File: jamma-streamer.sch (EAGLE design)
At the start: 49 parts, among them IC1 LM7805, J1 Audio line out, J2 ICSP, J3 SDCARD, J4 USB, T1 TY-145P, T2 TY-145P, U1 CD74HC165MD16-M, U2 ATMEGA328PB-AUR, U3 74HC4050D, U4 TLV757X / LP298X, U5 CD74HC165MD16-M, U6 CD74HC165MD16-M, U7 FT232RL, Y1 16MHz

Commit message: New version including RTC and better alim
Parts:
- added B1: S8411-45R, S8411R:S8411-45R
- added C11, C12, C13: 0.1uF/16V, CMS:KEMET-C1210C104K4J
- added C8: 10uF/10V, CMS:KEMET-C1210C106K8N
- added JP1: (no value), pinhead:PINHD-1X5
- added R6, R7, R8, R9: 10K, CMS:BOURNS-CRM2512AJW103ELF
- added SJ1: (no value), jumper:SJW
- added U10: LM358DTD8-M, LM358D:LM358DTD8-M
- added U8: DS3231SNT&R21-0042B_16-M, DS3231:DS3231SNT&R21-0042B_16-M
- added U9: NDT2955SOT-223-M, NDT2955:NDT2955SOT-223-M
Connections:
- net N$13 renamed PB6
- removed net N$11: C7.P$2, U7.3V3OUT
- new net CMD_GATE: U10.2IN-, U10.2OUT, U9.G
- new net CMP: C12.P$1, R8.P$1, R9.P$2, U10.1IN+
- new net DTR: C11.P$1, JP1.4, U7.DTR
- new net N$13: C11.P$2, SJ1.1
- new net N$31: B1.+, U8.VBAT
- new net PB7: C2.P$1, U2.PB7, Y1.1
- new net RTS: JP1.3, U7.RTS
- new net SCL: R6.P$2, U2.PC5, U8.SCL
- new net SDA: R7.P$2, U2.PC4, U8.SDA
- new net USBVCC: C10.P$1, C9.P$1, F1.P$2, U7.VCC, U9.D
- new net VCC33: C7.P$2, U10.1IN-, U7.3V3OUT
- new net VIN: C5.P$1, D5.P$1, IC1.VI, R8.P$2
- net CS: now also JP1.5; no longer C2.P$1, U2.PB7, Y1.1
- net FTDI_RXD: now also JP1.2
- net FTDI_TXD: now also JP1.1
- net GND: now also B1.-, C12.P$2, C13.P$2, C8.P$2, R9.P$1, U10.GND, U8.GND
- net JAMMA+12V: now also D5.P$2; no longer C5.P$1, IC1.VI
- net N$23: now also U10.1OUT, U10.2IN+; no longer D5.P$2, IC1.VO
- net RESET: now also SJ1.2
- net VCC: now also C13.P$1, C8.P$1, IC1.VO, R6.P$1, R7.P$1, U10.VCC, U8.VCC, U9.S; no longer C10.P$1, C9.P$1, D5.P$1, F1.P$2, U7.VCC
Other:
- note added: "CS = PB2 = Pin 10 Used to send reset signal when using ISP if using this atmega to program others"
- note added: "In the arduino code: Pin0=d0 Pin1 = d1 Pin2 = d2 ..."
- note added: "In the arduino code: Pin16=d0 Pin17 = d1 Pin18 = d2 ..."
- note added: "In the arduino code: Pin8=d0 Pin9 = d1 Pin10 = d2 ..."

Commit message: Updating readme with more info
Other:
- note added: "CS = PB2 = Pin 10 Used by ArduinoISP sketch to send a reset signal when using this atmega as ISP programmer"
- note added: "In the arduino code: Pin0 = d0 Pin1 = d1 Pin2 = d2 ..."
- note added: "In the arduino code: Pin16 = d0 Pin17 = d1 Pin18 = d2 ..."
- note added: "In the arduino code: Pin8 = d0 Pin9 = d1 Pin10 = d2 ..."
- note added: "MISO SCK RST"
- note added: "VCC MOSI GND"
- note removed: "CS = PB2 = Pin 10 Used to send reset signal when using ISP if using this atmega to program others"
- note removed: "In the arduino code: Pin0=d0 Pin1 = d1 Pin2 = d2 ..."
- note removed: "In the arduino code: Pin16=d0 Pin17 = d1 Pin18 = d2 ..."
- note removed: "In the arduino code: Pin8=d0 Pin9 = d1 Pin10 = d2 ..."
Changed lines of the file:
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@@
 <?xml version="1.0" encoding="utf-8"?>
 <!DOCTYPE eagle SYSTEM "eagle.dtd">
-<eagle version="9.2.2">
+<eagle version="9.6.2">
 <drawing>
 <settings>
@@
 PD6 = Data
 PD7 = Clock</text>
+<text x="7.62" y="106.68" size="1.778" layer="91">MISO
+SCK
+RST</text>
+<text x="20.32" y="106.68" size="1.778" layer="91">VCC
+MOSI
+GND</text>
 </plain>
 <instances>
@@
 <segment>
 <pinref part="SUPPLY9" gate="G$1" pin="VCC"/>
-<wire x1="111.76" y1="101.6" x2="111.76" y2="106.68" width="0.1524" layer="91"/>
+<wire x1="111.76" y1="99.06" x2="111.76" y2="106.68" width="0.1524" layer="91"/>
 <pinref part="U2" gate="G$1" pin="VCC"/>
 <wire x1="91.44" y1="99.06" x2="99.06" y2="99.06" width="0.1524" layer="91"/>
 <wire x1="99.06" y1="99.06" x2="111.76" y2="99.06" width="0.1524" layer="91"/>
-<wire x1="111.76" y1="99.06" x2="111.76" y2="101.6" width="0.1524" layer="91"/>
 <pinref part="U2" gate="G$1" pin="AVCC"/>
 <wire x1="91.44" y1="101.6" x2="99.06" y2="101.6" width="0.1524" layer="91"/>
@@
 <text x="-45.72" y="207.01" size="1.778" layer="91" font="vector">Jamma is HIGH when not pressed (~3V)
 and LOW when pressed !</text>
-<text x="96.52" y="119.38" size="1.27" layer="91">In the arduino code:
-Pin0=d0
+<text x="96.52" y="119.38" size="1.27" layer="91" font="fixed">In the arduino code:
+Pin0 = d0
 Pin1 = d1
 Pin2 = d2
 ...</text>
-<text x="99.06" y="160.02" size="1.27" layer="91">In the arduino code:
-Pin8=d0
-Pin9 = d1
+<text x="99.06" y="160.02" size="1.27" layer="91" font="fixed">In the arduino code:
+Pin8  = d0
+Pin9  = d1
 Pin10 = d2
 ...</text>
-<text x="88.9" y="200.66" size="1.27" layer="91">In the arduino code:
-Pin16=d0
+<text x="88.9" y="200.66" size="1.27" layer="91" font="fixed">In the arduino code:
+Pin16 = d0
 Pin17 = d1
 Pin18 = d2
@@
 <description>USB input</description>
 <plain>
-<text x="104.14" y="76.2" size="1.778" layer="91">CS = PB2 = Pin 10
-Used to send reset signal when using ISP
-if using this atmega to program others</text>
+<text x="104.14" y="73.66" size="1.778" layer="91">CS = PB2 = Pin 10
+Used by ArduinoISP sketch to send a reset
+signal when using this atmega as ISP programmer</text>
 </plain>
 <instances>

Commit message: New README, new schematic after burn fixing
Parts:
- SJ1: device jumper:SJW -> jumper:SJ
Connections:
- removed net VCCIO: R4.P$2, R5.P$2, U7.VCCIO
- net USBVCC: now also R4.P$2, R5.P$2, U7.VCCIO
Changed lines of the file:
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@@
 <layer number="1" name="Top" color="4" fill="1" visible="no" active="no"/>
 <layer number="2" name="Route2" color="16" fill="1" visible="no" active="no"/>
+<layer number="3" name="Route3" color="4" fill="3" visible="no" active="no"/>
+<layer number="4" name="Route4" color="1" fill="4" visible="no" active="no"/>
+<layer number="5" name="Route5" color="4" fill="4" visible="no" active="no"/>
+<layer number="6" name="Route6" color="1" fill="8" visible="no" active="no"/>
+<layer number="7" name="Route7" color="4" fill="8" visible="no" active="no"/>
+<layer number="8" name="Route8" color="1" fill="2" visible="no" active="no"/>
+<layer number="9" name="Route9" color="4" fill="2" visible="no" active="no"/>
+<layer number="10" name="Route10" color="1" fill="7" visible="no" active="no"/>
+<layer number="11" name="Route11" color="4" fill="7" visible="no" active="no"/>
+<layer number="12" name="Route12" color="1" fill="5" visible="no" active="no"/>
+<layer number="13" name="Route13" color="4" fill="5" visible="no" active="no"/>
+<layer number="14" name="Route14" color="1" fill="6" visible="no" active="no"/>
 <layer number="15" name="Route15" color="23" fill="1" visible="no" active="no"/>
 <layer number="16" name="Bottom" color="1" fill="1" visible="no" active="no"/>
@@
 <part name="R5" library="CMS" deviceset="BOURNS-652CHP0603FX1001ELF" device="" value="1K"/>
 <part name="D4-TX" library="CMS" deviceset="604-APTD1608LCGCK" device="" value="Green"/>
-<part name="SUPPLY16" library="SparkFun-PowerSymbols" library_urn="urn:adsk.eagle:library:530" deviceset="VCCIO" device=""/>
-<part name="SUPPLY17" library="SparkFun-PowerSymbols" library_urn="urn:adsk.eagle:library:530" deviceset="VCCIO" device=""/>
 <part name="D5" library="RRE07VTM4SFHTR" deviceset="RRE07VTM4SFHTR" device="" value="RRE07VTM4SFHTR"/>
 <part name="GND24" library="SparkFun-PowerSymbols" library_urn="urn:adsk.eagle:library:530" deviceset="GND" device=""/>
@@
 <part name="C11" library="CMS" deviceset="KEMET-C1210C104K4J" device="" value="0.1uF/16V"/>
 <part name="JP1" library="pinhead" library_urn="urn:adsk.eagle:library:325" deviceset="PINHD-1X5" device="" package3d_urn="urn:adsk.eagle:package:22469/2"/>
-<part name="SJ1" library="jumper" library_urn="urn:adsk.eagle:library:252" deviceset="SJ" device="W" package3d_urn="urn:adsk.eagle:package:15507/1"/>
+<part name="SJ1" library="jumper" library_urn="urn:adsk.eagle:library:252" deviceset="SJ" device="" package3d_urn="urn:adsk.eagle:package:15471/1"/>
 <part name="U8" library="DS3231" deviceset="DS3231SNT&amp;R" device="21-0042B_16-M"/>
 <part name="SUPPLY18" library="SparkFun-PowerSymbols" library_urn="urn:adsk.eagle:library:530" deviceset="VCC" device=""/>
@@
 <part name="GND33" library="SparkFun-PowerSymbols" library_urn="urn:adsk.eagle:library:530" deviceset="GND" device=""/>
 <part name="SUPPLY22" library="SparkFun-PowerSymbols" library_urn="urn:adsk.eagle:library:530" deviceset="VCC" device=""/>
+<part name="SUPPLY23" library="SparkFun-PowerSymbols" library_urn="urn:adsk.eagle:library:530" deviceset="VCCIO" device=""/>
 </parts>
 <sheets>
@@
 <attribute name="VALUE" x="116.84" y="48.26" size="2.032" layer="94" rot="R180"/>
 </instance>
-<instance part="SUPPLY16" gate="G$1" x="137.16" y="43.18" smashed="yes" rot="R270">
-<attribute name="VALUE" x="139.954" y="43.18" size="1.778" layer="96" rot="R270" align="bottom-center"/>
-</instance>
-<instance part="SUPPLY17" gate="G$1" x="137.16" y="27.94" smashed="yes" rot="R270">
-<attribute name="VALUE" x="139.954" y="27.94" size="1.778" layer="96" rot="R270" align="bottom-center"/>
-</instance>
 <instance part="C11" gate="A" x="114.3" y="50.8" smashed="yes" rot="R180">
 <attribute name="NAME" x="117.3" y="49.3" size="1.27" layer="94" rot="R180"/>
@@
 <attribute name="NAME" x="124.46" y="53.34" size="1.778" layer="95"/>
 <attribute name="VALUE" x="124.46" y="46.99" size="1.778" layer="96"/>
+</instance>
+<instance part="SUPPLY23" gate="G$1" x="15.24" y="12.7" smashed="yes" rot="R90">
+<attribute name="VALUE" x="12.446" y="12.7" size="1.778" layer="96" rot="R90" align="bottom-center"/>
 </instance>
 </instances>
@@
 </segment>
 </net>
-<net name="VCCIO" class="0">
-<segment>
-<pinref part="U7" gate="G$1" pin="VCCIO"/>
-<wire x1="68.58" y1="50.8" x2="68.58" y2="48.26" width="0.1524" layer="91"/>
-<wire x1="68.58" y1="48.26" x2="66.04" y2="48.26" width="0.1524" layer="91"/>
-<label x="66.04" y="48.26" size="1.27" layer="95" rot="R180" xref="yes"/>
-</segment>
-<segment>
-<pinref part="R5" gate="A" pin="P$2"/>
-<wire x1="133" y1="43.18" x2="137.16" y2="43.18" width="0.1524" layer="91"/>
-<pinref part="SUPPLY16" gate="G$1" pin="VCCIO"/>
-</segment>
-<segment>
-<pinref part="R4" gate="A" pin="P$2"/>
-<wire x1="133" y1="27.94" x2="137.16" y2="27.94" width="0.1524" layer="91"/>
-<pinref part="SUPPLY17" gate="G$1" pin="VCCIO"/>
-</segment>
-</net>
 <net name="N$8" class="0">
 <segment>
@@
 <segment>
 <pinref part="SJ1" gate="1" pin="2"/>
-<wire x1="132.08" y1="50.8" x2="134.62" y2="50.8" width="0.1524" layer="91"/>
-<label x="134.62" y="50.8" size="1.27" layer="95" xref="yes"/>
+<wire x1="132.08" y1="50.8" x2="137.16" y2="50.8" width="0.1524" layer="91"/>
+<label x="137.16" y="50.8" size="1.27" layer="95" xref="yes"/>
 </segment>
 </net>
@@
 <net name="USBVCC" class="0">
 <segment>
+<pinref part="U7" gate="G$1" pin="VCCIO"/>
+<wire x1="68.58" y1="50.8" x2="68.58" y2="48.26" width="0.1524" layer="91"/>
 <pinref part="C9" gate="A" pin="P$1"/>
 <pinref part="F1" gate="A" pin="P$2"/>
 <wire x1="38.1" y1="50.8" x2="43.18" y2="50.8" width="0.1524" layer="91"/>
-<wire x1="43.18" y1="50.8" x2="43.18" y2="46.172" width="0.1524" layer="91"/>
+<wire x1="43.18" y1="50.8" x2="43.18" y2="48.26" width="0.1524" layer="91"/>
 <junction x="43.18" y="50.8"/>
 <pinref part="C10" gate="A" pin="P$1"/>
+<wire x1="43.18" y1="48.26" x2="43.18" y2="46.172" width="0.1524" layer="91"/>
 <wire x1="50.8" y1="50.8" x2="43.18" y2="50.8" width="0.1524" layer="91"/>
 <wire x1="50.8" y1="46.172" x2="50.8" y2="50.8" width="0.1524" layer="91"/>
@@
 <junction x="43.18" y="50.8"/>
 <label x="43.18" y="66.04" size="1.27" layer="95" rot="R90" xref="yes"/>
-</segment>
-</net>
+<wire x1="68.58" y1="48.26" x2="43.18" y2="48.26" width="0.1524" layer="91"/>
+<junction x="43.18" y="48.26"/>
+</segment>
+<segment>
+<pinref part="R5" gate="A" pin="P$2"/>
+<wire x1="133" y1="43.18" x2="134.62" y2="43.18" width="0.1524" layer="91"/>
+<pinref part="R4" gate="A" pin="P$2"/>
+<wire x1="134.62" y1="43.18" x2="134.62" y2="35.56" width="0.1524" layer="91"/>
+<wire x1="134.62" y1="35.56" x2="134.62" y2="27.94" width="0.1524" layer="91"/>
+<wire x1="134.62" y1="27.94" x2="133" y2="27.94" width="0.1524" layer="91"/>
+<wire x1="134.62" y1="35.56" x2="137.16" y2="35.56" width="0.1524" layer="91"/>
+<junction x="134.62" y="35.56"/>
+<label x="137.16" y="35.56" size="1.27" layer="95" xref="yes"/>
+</segment>
+</net>

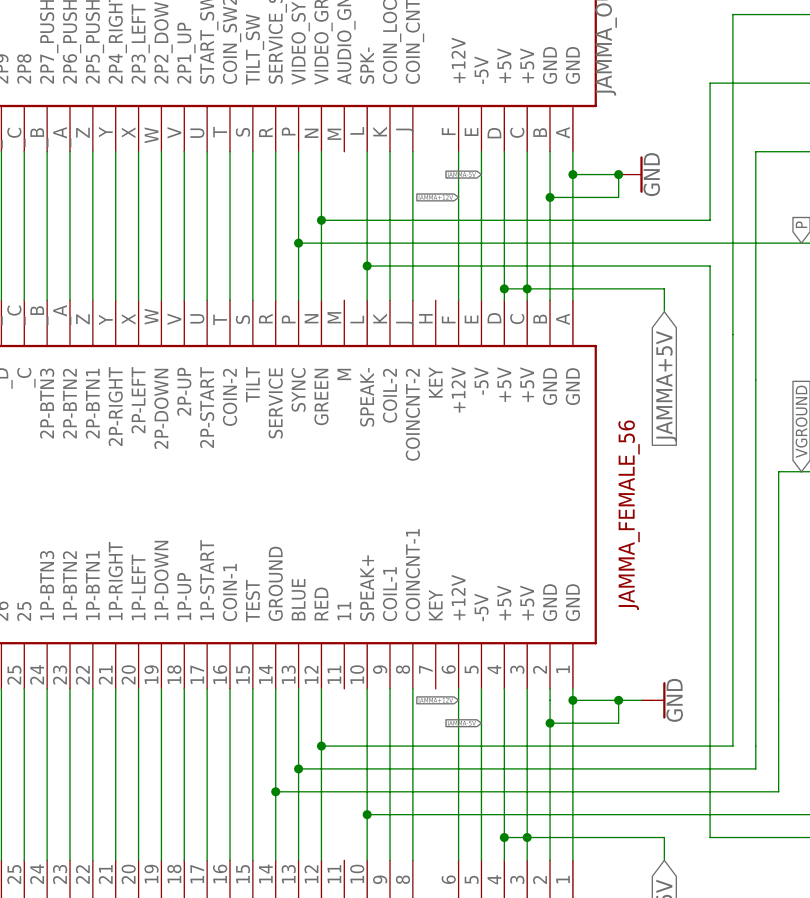
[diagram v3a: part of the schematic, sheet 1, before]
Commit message: Added buttons detection atmega code
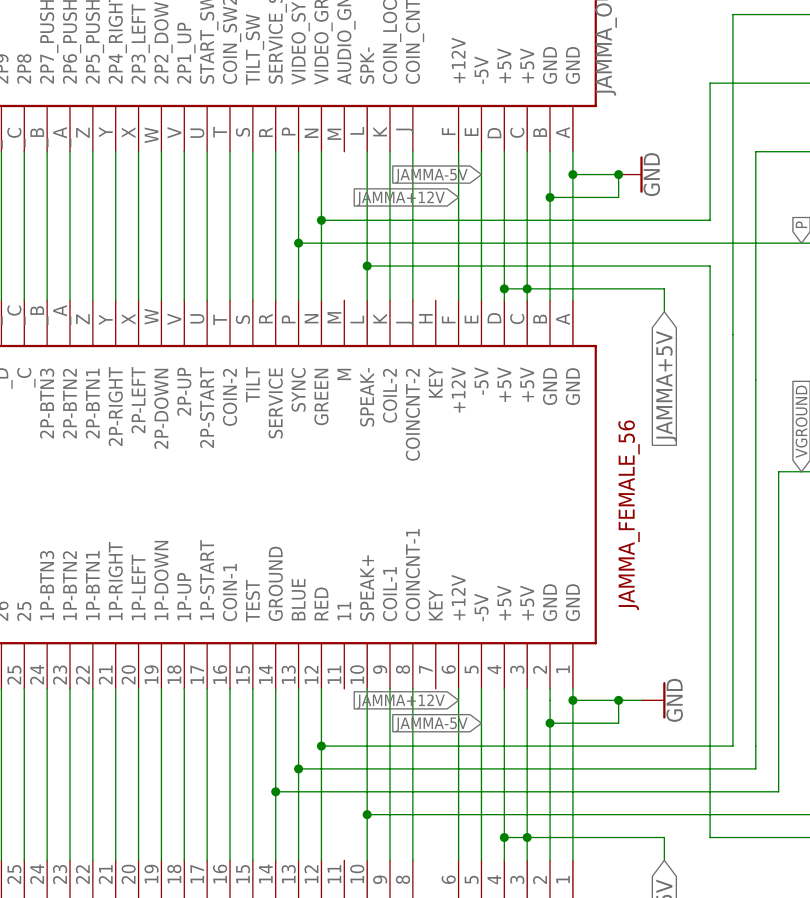
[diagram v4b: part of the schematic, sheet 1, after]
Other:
- note added: "Jamma is HIGH when not pressed (~5V) and LOW when pressed !"
- note added: "VIN from jamma +12V"
- note removed: "Jamma is HIGH when not pressed (~3V) and LOW when pressed !"
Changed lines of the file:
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@@
 <pinref part="JAMMA_OUT_TOP" gate="G$1" pin="+12V"/>
 <wire x1="71.12" y1="95.25" x2="71.12" y2="76.2" width="0.1524" layer="91"/>
-<label x="71.12" y="93.98" size="0.508" layer="95" font="vector" rot="R180" xref="yes"/>
+<label x="71.12" y="93.98" size="1.27" layer="95" font="vector" rot="R180" xref="yes"/>
 </segment>
 <segment>
@@
 <pinref part="JAMMA_IN" gate="G$1" pin="+12V@F"/>
 <wire x1="71.12" y1="154.94" x2="71.12" y2="138.43" width="0.1524" layer="91"/>
-<label x="71.12" y="149.86" size="0.508" layer="95" font="vector" rot="R180" xref="yes"/>
+<label x="71.12" y="149.86" size="1.27" layer="95" font="vector" rot="R180" xref="yes"/>
 </segment>
 </net>
@@
 <pinref part="JAMMA_IN" gate="G$1" pin="-5V@E"/>
 <wire x1="73.66" y1="154.94" x2="73.66" y2="138.43" width="0.1524" layer="91"/>
-<label x="73.66" y="152.4" size="0.508" layer="95" font="vector" rot="R180" xref="yes"/>
+<label x="73.66" y="152.4" size="1.27" layer="95" font="vector" rot="R180" xref="yes"/>
 </segment>
 <segment>
@@
 <pinref part="JAMMA_IN" gate="G$1" pin="-5V@5"/>
 <wire x1="73.66" y1="76.2" x2="73.66" y2="95.25" width="0.1524" layer="91"/>
-<label x="73.66" y="91.44" size="0.508" layer="95" font="vector" rot="R180" xref="yes"/>
+<label x="73.66" y="91.44" size="1.27" layer="95" font="vector" rot="R180" xref="yes"/>
 </segment>
 </net>
@@
 <description>Alimentation 12V -&gt; 5V -&gt; 3.3V</description>
 <plain>
+<text x="2.54" y="142.24" size="1.778" layer="91">VIN from jamma +12V</text>
 </plain>
 <instances>
@@
 <description>Buttons detection</description>
 <plain>
-<text x="-45.72" y="207.01" size="1.778" layer="91" font="vector">Jamma is HIGH when not pressed (~3V)
+<text x="-45.72" y="207.01" size="1.778" layer="91" font="vector">Jamma is HIGH when not pressed (~5V)
 and LOW when pressed !</text>
 <text x="96.52" y="119.38" size="1.27" layer="91" font="fixed">In the arduino code:

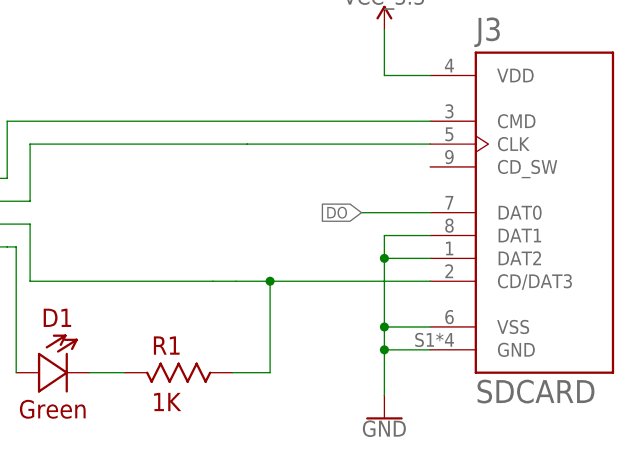
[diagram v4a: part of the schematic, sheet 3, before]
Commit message: Added Arduino pinout diagram
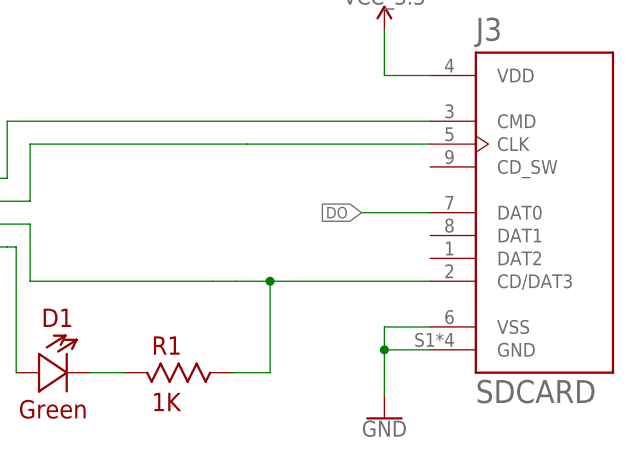
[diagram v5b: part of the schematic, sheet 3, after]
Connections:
- net N$14 renamed SD_CS
- net N$15 renamed SD_CMD
- net N$17 renamed SD_CLK
- net GND: no longer J3.DAT1, J3.DAT2
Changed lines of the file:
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@@
 <wire x1="96.52" y1="10.16" x2="96.52" y2="7.62" width="0.1524" layer="91"/>
 <junction x="96.52" y="7.62"/>
-<pinref part="J3" gate="G$1" pin="DAT1"/>
-<wire x1="101.6" y1="20.32" x2="96.52" y2="20.32" width="0.1524" layer="91"/>
-<wire x1="96.52" y1="20.32" x2="96.52" y2="17.78" width="0.1524" layer="91"/>
-<junction x="96.52" y="10.16"/>
-<pinref part="J3" gate="G$1" pin="DAT2"/>
-<wire x1="96.52" y1="17.78" x2="96.52" y2="10.16" width="0.1524" layer="91"/>
-<wire x1="101.6" y1="17.78" x2="96.52" y2="17.78" width="0.1524" layer="91"/>
-<junction x="96.52" y="17.78"/>
 </segment>
 <segment>
@@
 </segment>
 </net>
-<net name="N$15" class="0">
+<net name="SD_CMD" class="0">
 <segment>
 <pinref part="U3" gate="G$1" pin="1Y"/>
@@
 </segment>
 </net>
-<net name="N$17" class="0">
+<net name="SD_CLK" class="0">
 <segment>
 <pinref part="U3" gate="G$1" pin="2Y"/>
@@
 </segment>
 </net>
-<net name="N$14" class="0">
+<net name="SD_CS" class="0">
 <segment>
 <pinref part="J3" gate="G$1" pin="CD/DAT3"/>
